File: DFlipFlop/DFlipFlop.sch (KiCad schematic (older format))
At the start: 5 parts, among them U1 74LS08, U2 74LS08, U3 74LS02, U4 74LS04

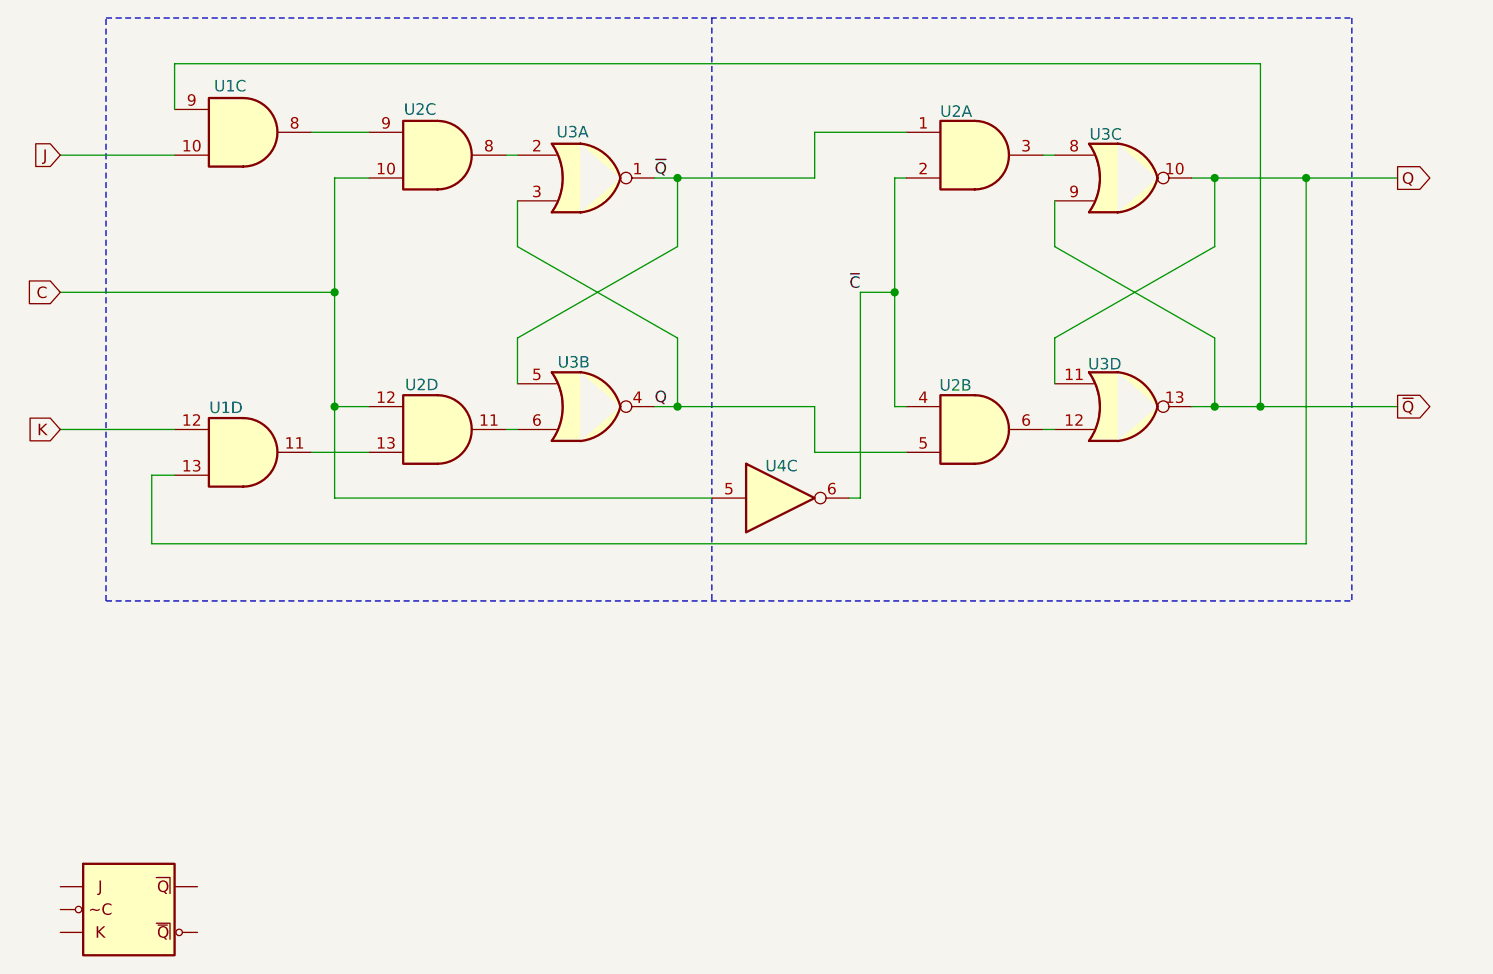
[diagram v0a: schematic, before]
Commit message: add D and T Latch
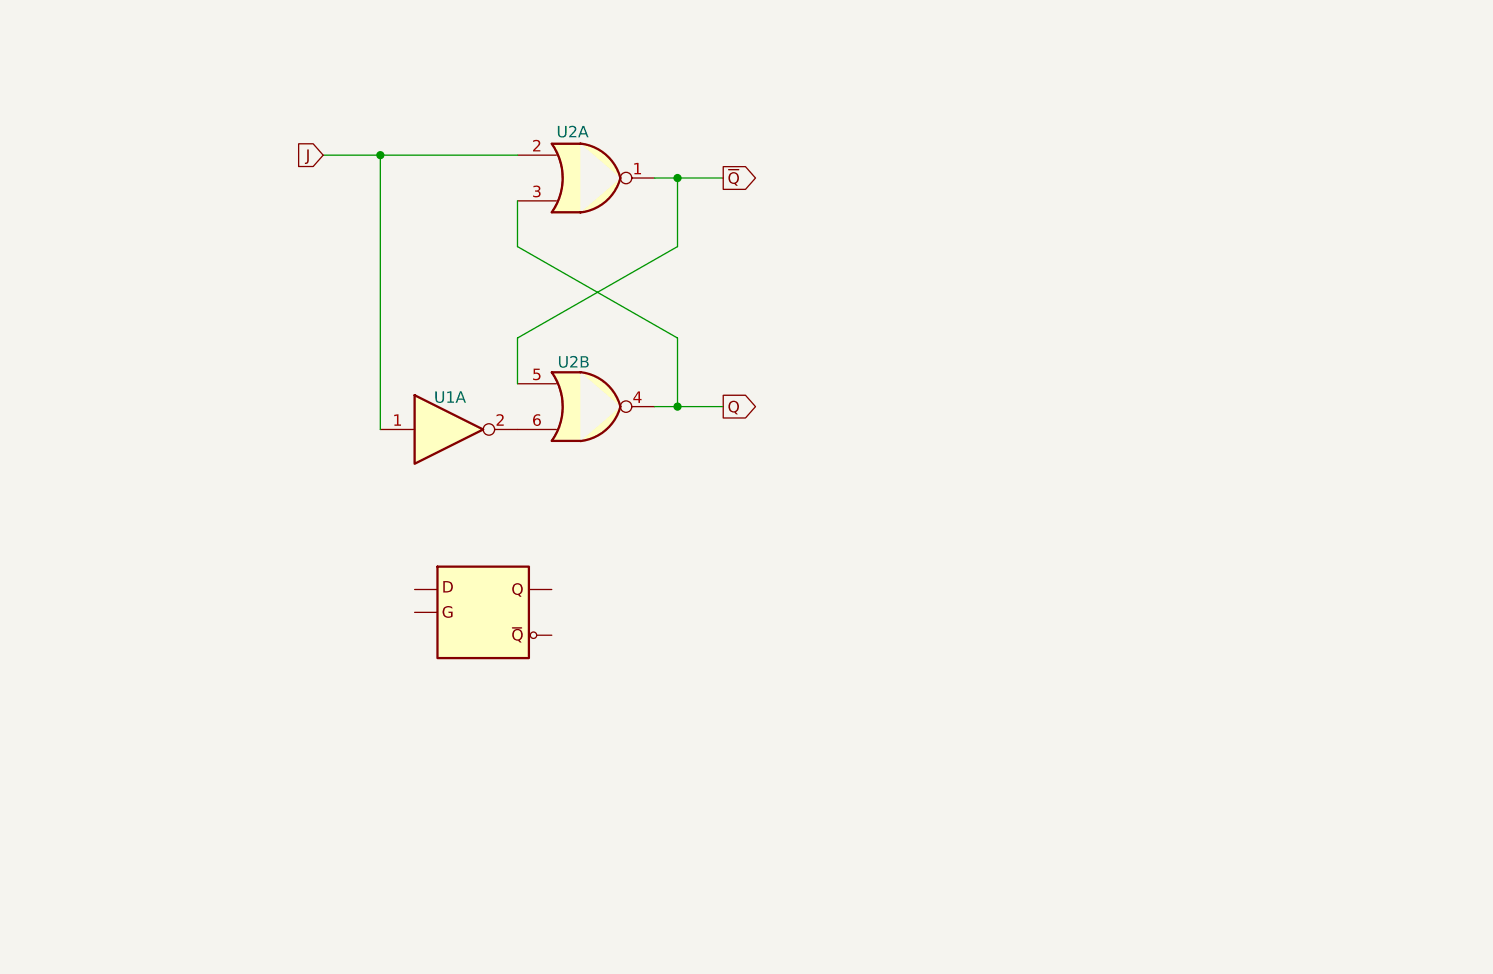
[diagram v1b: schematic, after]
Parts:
- removed U1, U2: 74LS08, symbol 74xx:74LS08
- removed unit 4 of U3
- removed unit 3 of U3
- removed U?: JK_MS, symbol 00TJR:JK_MS
- added U?: D_Latch, symbol 00TJR:D_Latch
- renumbered U4 to U1, U3 to U2
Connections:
- net J: now also U1.1, U2.2
- net at U2.6: now also U1.2
- removed net C: U1.5
- removed net ~C: U1.6

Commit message: start clean up
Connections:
- net J renamed D
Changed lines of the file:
@@
 $EndComp
 Text GLabel 4100 3150 0    50   Input ~ 0
-J
+D
 Wire Wire Line
 	4350 3150 4350 4350
